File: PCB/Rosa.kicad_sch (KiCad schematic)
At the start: 2 parts, among them U1 XC9572XL-TQ100, U2 AMBER

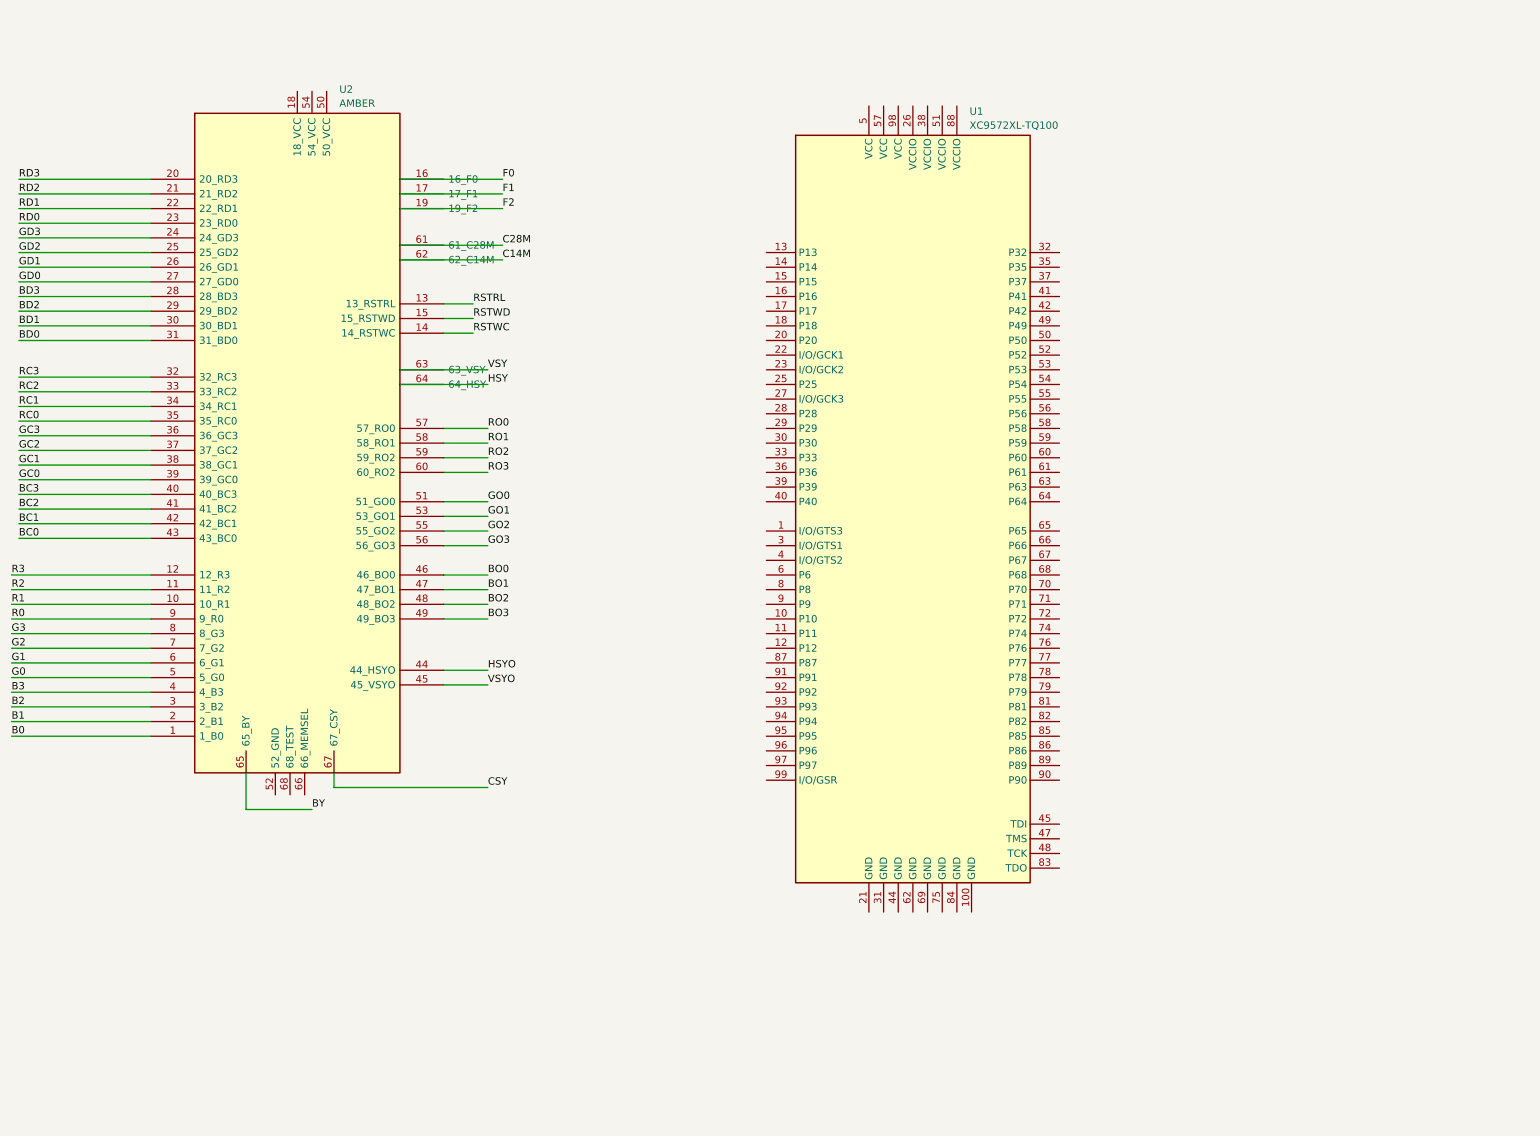
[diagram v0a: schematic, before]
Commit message: Add files via upload
Partial schematics updated.  Lacks most of the IO pin routing.
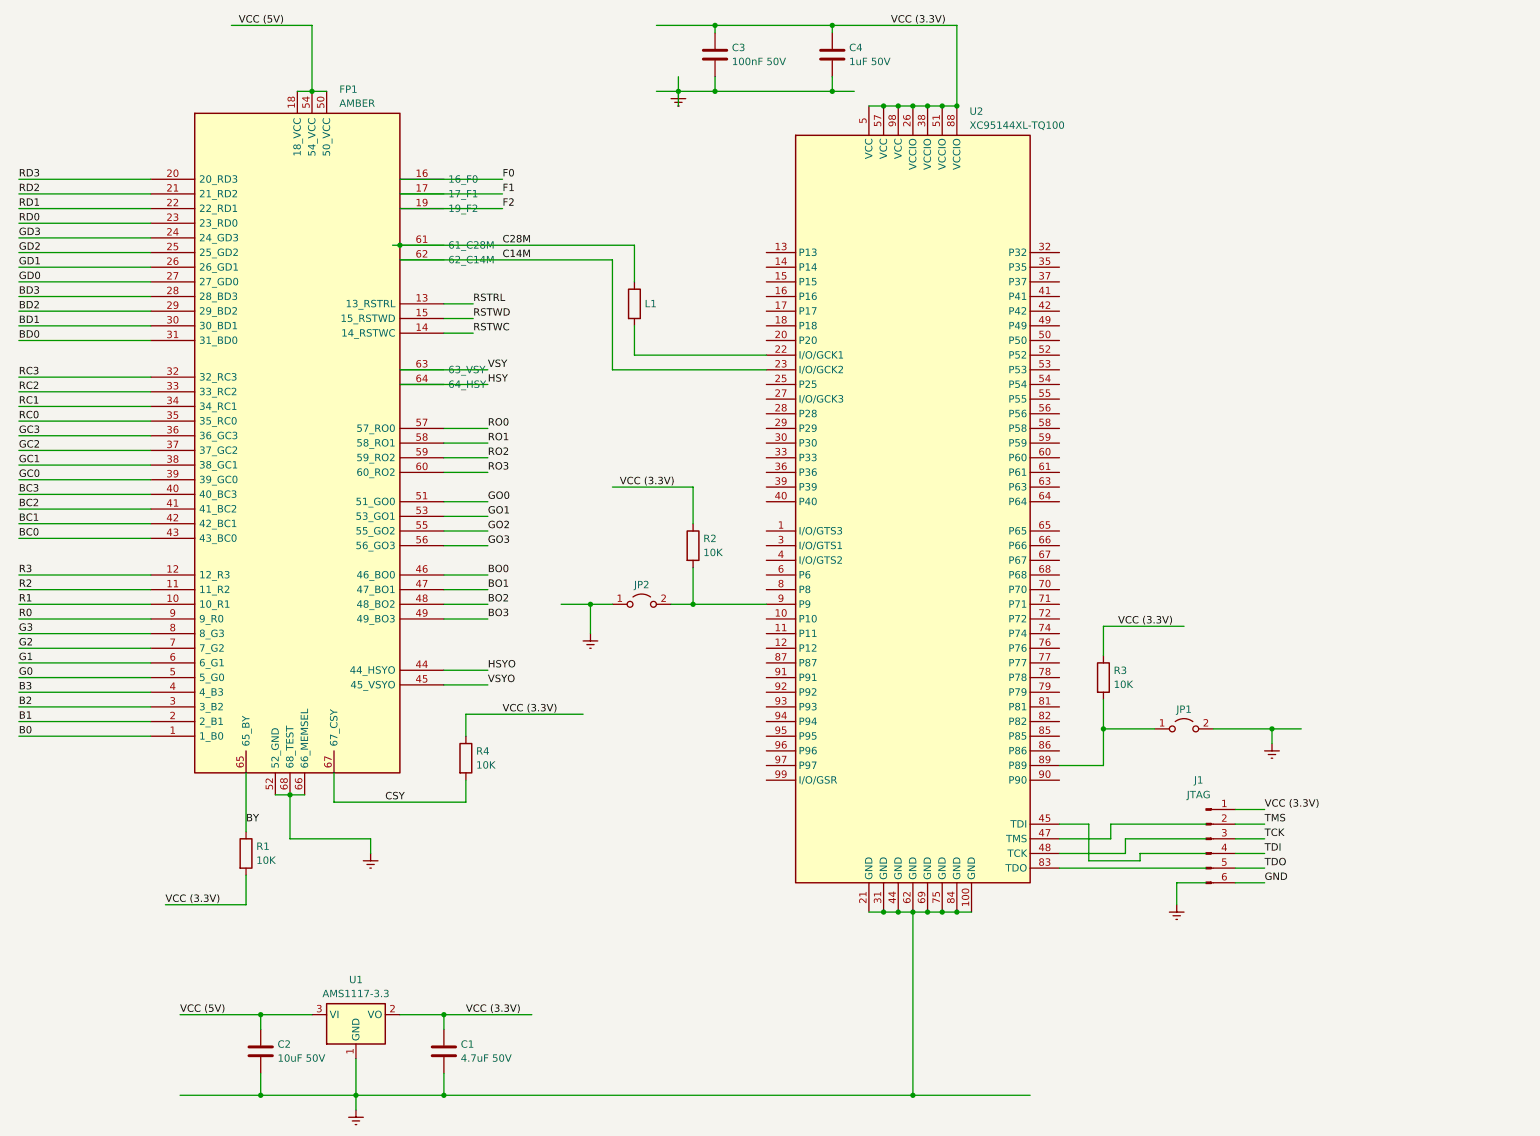
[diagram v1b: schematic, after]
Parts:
- added C1: 4.7uF 50V, symbol Device:C
- added C2: 10uF 50V, symbol Device:C
- added C3: 100nF 50V, symbol Device:C
- added C4: 1uF 50V, symbol Device:C
- added J1: JTAG, symbol Connector:Conn_01x06_Pin
- added JP1, JP2: ~, symbol Jumper:Jumper_2_Open
- added L1: ~, symbol Device:R
- added R1, R2, R3, R4: 10K, symbol Device:R
- added U1: AMS1117-3.3, Package_TO_SOT_SMD:SOT-223-3_TabPin2, symbol Regulator_Linear:AMS1117-3.3
- U2: renamed from U1; value XC9572XL-TQ100 -> XC95144XL-TQ100
- renumbered U2 to FP1
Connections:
- net BY: now also R1.1
- net C14M: now also U2.23 (I/O/GCK2)
- net C28M: now also L1.1
- net CSY: now also R4.2
- net VCC (5V): now reaches FP1.18 (18_VCC)
- net VCC (5V): now also FP1.50 (50_VCC), FP1.54 (54_VCC), C2.1, U1.3 (VI)
- net Earth: now reaches FP1.52 (52_GND)
- net Earth: now also FP1.66 (66_MEMSEL), FP1.68 (68_TEST), U2.100 (GND), U2.21 (GND), U2.31 (GND), U2.44 (GND), U2.62 (GND), U2.69 (GND), U2.75 (GND), U2.84 (GND), C1.2, C2.2, C3.2, C4.2, JP1.2 (B), JP2.1 (A), U1.1 (GND)
- net at U2.22 (I/O/GCK1): now also L1.2
- net VCC (3.3V): now reaches U2.26 (VCCIO)
- net VCC (3.3V): now also U2.38 (VCCIO), U2.5 (VCC), U2.51 (VCCIO), U2.57 (VCC), U2.88 (VCCIO), U2.98 (VCC), C1.1, C3.1, C4.1, J1.1 (Pin_1), R1.2, R2.1, R3.1, R4.1, U1.2 (VO)
- net at U2.89 (P89): now also JP1.1 (A), R3.2
- net at U2.9 (P9): now also JP2.2 (B), R2.2
- new net GND: J1.6 (Pin_6)
- new net TCK: J1.3 (Pin_3)
- new net TDI: J1.4 (Pin_4)
- new net TDO: J1.5 (Pin_5)
- new net TMS: J1.2 (Pin_2)
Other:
- title: (none) -> Marine (Partial Schematics)

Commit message: Add files via upload
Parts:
- FP1: value AMBER -> AMBER SOCKET
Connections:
- net HSY is gone; now on net HSY (HSYNC IN): FP1.64 (64_HSY)
- net HSYO is gone; now on net HSYO (HSYNC OUT): FP1.44 (44_HSYO)
- net VSY is gone; now on net VSY (VSYNC IN): FP1.63 (63_VSY)
- net VSYO is gone; now on net VSYO (VSYNC OUT): FP1.45 (45_VSYO)
- net B0: now also U2.32 (P32)
- net B1: now also U2.35 (P35)
- net B2: now also U2.37 (P37)
- net B3: now also U2.39 (P39)
- net BC0: now also U2.97 (P97)
- net BC1: now also U2.99 (I/O/GSR)
- net BC2: now also U2.96 (P96)
- net BC3: now also U2.91 (P91)
- net BD0: now also U2.86 (P86)
- net BD1: now also U2.81 (P81)
- net BD2: now also U2.79 (P79)
- net BD3: now also U2.78 (P78)
- net BO0: now also U2.4 (I/O/GTS2)
- net BO1: now also U2.1 (I/O/GTS3)
- net BO2: now also U2.13 (P13)
- net BO3: now also U2.6 (P6)
- net BY: now also U2.29 (P29)
- net CSY: now also U2.30 (P30)
- net F0: now also U2.64 (P64)
- net F1: now also U2.63 (P63)
- net F2: now also U2.66 (P66)
- net G0: now also U2.40 (P40)
- net G1: now also U2.41 (P41)
- net G2: now also U2.36 (P36)
- net G3: now also U2.42 (P42)
- net GC0: now also U2.95 (P95)
- net GC1: now also U2.94 (P94)
- net GC2: now also U2.93 (P93)
- net GC3: now also U2.92 (P92)
- net GD0: now also U2.77 (P77)
- net GD1: now also U2.76 (P76)
- net GD2: now also U2.74 (P74)
- net GD3: now also U2.72 (P72)
- net GO0: now also U2.14 (P14)
- net GO1: now also U2.15 (P15)
- net GO2: now also U2.17 (P17)
- net GO3: now also U2.16 (P16)
- net R0: now also U2.58 (P58)
- net R1: now also U2.50 (P50)
- net R2: now also U2.49 (P49)
- net R3: now also U2.61 (P61)
- net RC0: now also U2.90 (P90)
- net RC1: now also U2.87 (P87)
- net RC2: now also U2.85 (P85)
- net RC3: now also U2.82 (P82)
- net RD0: now also U2.71 (P71)
- net RD1: now also U2.70 (P70)
- net RD2: now also U2.68 (P68)
- net RD3: now also U2.67 (P67)
- net RO0: now also U2.20 (P20)
- net RO1: now also U2.18 (P18)
- net RO2: now also U2.25 (P25)
- net RO3: now also U2.12 (P12)
- net RSTRL: now also U2.52 (P52)
- net RSTWC: now also U2.60 (P60)
- net RSTWD: now also U2.56 (P56)
- net HSY (HSYNC IN): now reaches U2.27 (I/O/GCK3)
- net VSY (VSYNC IN): now reaches U2.28 (P28)
- net VSYO (VSYNC OUT): now reaches U2.3 (I/O/GTS1)
- net HSYO (HSYNC OUT): now reaches U2.8 (P8)
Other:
- moved on the sheet: JP1, JP2, R2, R3, R4
